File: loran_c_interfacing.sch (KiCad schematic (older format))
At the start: 17 parts, among them P401 SPI Bus A, P402 SPI Bus B, U103 74AC14, U401 74AC14, U402 74AC14

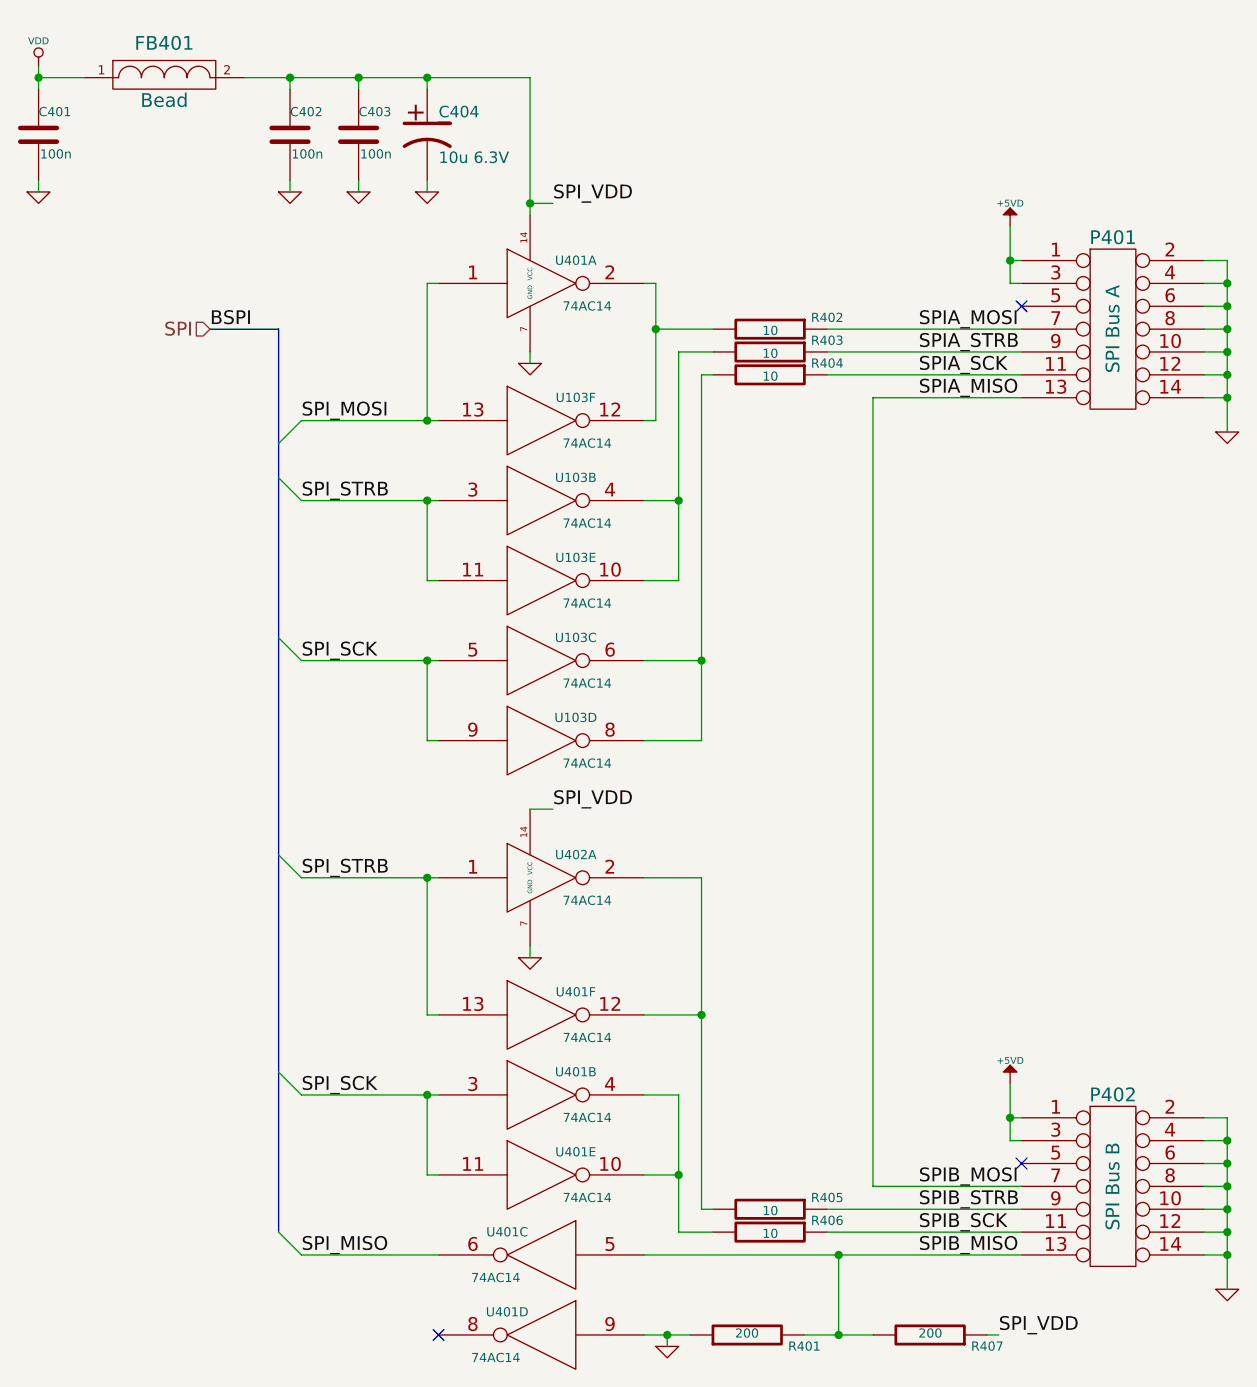
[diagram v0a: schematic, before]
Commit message: FIXED: no more buses on hierarchical sheet ports
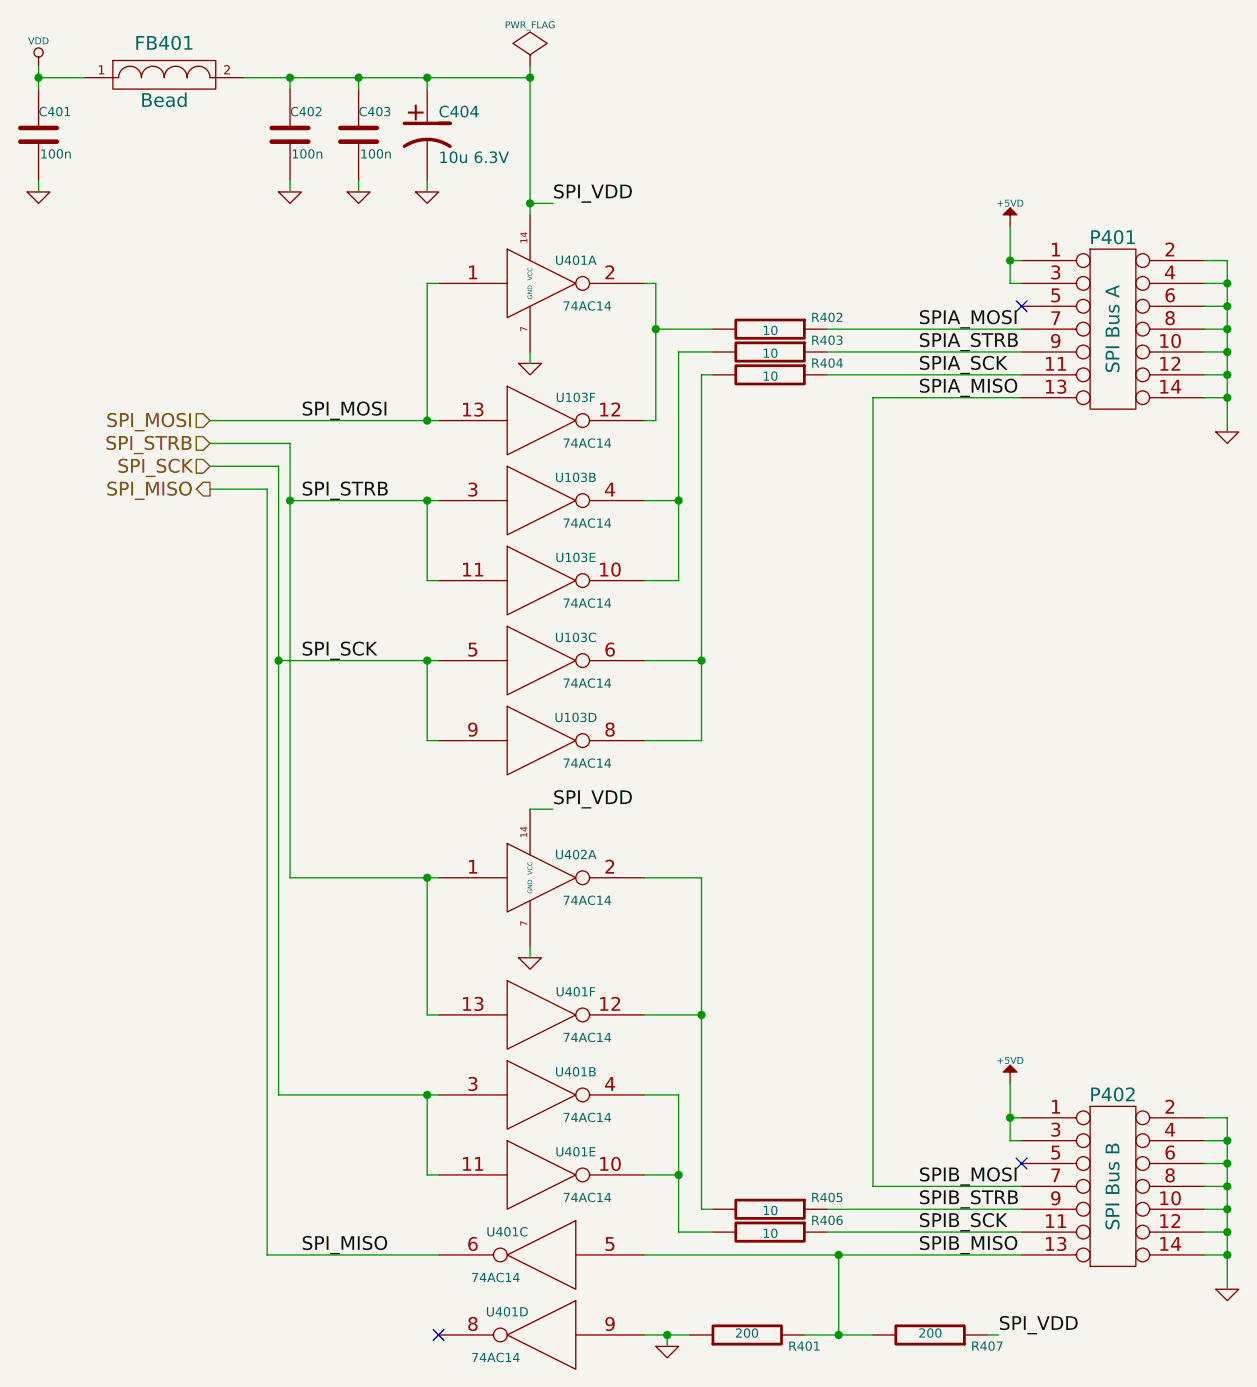
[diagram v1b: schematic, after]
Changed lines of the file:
@@
 $Descr A4 11693 8268
 encoding utf-8
-Sheet 4 7
+Sheet 3 7
 Title ""
 Date ""
@@
 $EndComp
 $Comp
-L GND #PWR066
+L GND #PWR058
 U 1 1 52DAD917
 P 8600 2350
-F 0 "#PWR066" H 8600 2350 30  0001 C CNN
+F 0 "#PWR058" H 8600 2350 30  0001 C CNN
 F 1 "GND" H 8600 2280 30  0001 C CNN
 F 2 "" H 8600 2350 60  0000 C CNN
@@
 $EndComp
 $Comp
-L +5VD #PWR067
+L +5VD #PWR059
 U 1 1 52DAE845
 P 7650 1450
-F 0 "#PWR067" H 7650 1400 20  0001 C CNN
+F 0 "#PWR059" H 7650 1400 20  0001 C CNN
 F 1 "+5VD" H 7650 1550 30  0000 C CNN
 F 2 "" H 7650 1450 60  0000 C CNN
@@
 $EndComp
 $Comp
-L GND #PWR068
+L GND #PWR060
 U 1 1 52DAF90C
 P 8600 6100
-F 0 "#PWR068" H 8600 6100 30  0001 C CNN
+F 0 "#PWR060" H 8600 6100 30  0001 C CNN
 F 1 "GND" H 8600 6030 30  0001 C CNN
 F 2 "" H 8600 6100 60  0000 C CNN
@@
 $EndComp
 $Comp
-L +5VD #PWR069
+L +5VD #PWR061
 U 1 1 52DAF91B
 P 7650 5200
-F 0 "#PWR069" H 7650 5150 20  0001 C CNN
+F 0 "#PWR061" H 7650 5150 20  0001 C CNN
 F 1 "+5VD" H 7650 5300 30  0000 C CNN
 F 2 "" H 7650 5200 60  0000 C CNN
@@
 $EndComp
 $Comp
-L GND #PWR070
+L GND #PWR062
 U 1 1 52DD7CC9
 P 5550 2050
-F 0 "#PWR070" H 5550 2050 30  0001 C CNN
+F 0 "#PWR062" H 5550 2050 30  0001 C CNN
 F 1 "GND" H 5550 1980 30  0001 C CNN
 F 2 "" H 5550 2050 60  0000 C CNN
@@
 $EndComp
 $Comp
-L GND #PWR071
+L GND #PWR063
 U 1 1 52DD892D
 P 5550 4650
-F 0 "#PWR071" H 5550 4650 30  0001 C CNN
+F 0 "#PWR063" H 5550 4650 30  0001 C CNN
 F 1 "GND" H 5550 4580 30  0001 C CNN
 F 2 "" H 5550 4650 60  0000 C CNN
@@
 $EndComp
 $Comp
-L GND #PWR072
+L GND #PWR064
 U 1 1 52DD8B76
 P 6150 6350
-F 0 "#PWR072" H 6150 6350 30  0001 C CNN
+F 0 "#PWR064" H 6150 6350 30  0001 C CNN
 F 1 "GND" H 6150 6280 30  0001 C CNN
 F 2 "" H 6150 6350 60  0000 C CNN
@@
 $EndComp
 $Comp
-L VDD #PWR073
+L VDD #PWR065
 U 1 1 52DDD53B
 P 3400 750
-F 0 "#PWR073" H 3400 850 30  0001 C CNN
+F 0 "#PWR065" H 3400 850 30  0001 C CNN
 F 1 "VDD" H 3400 860 30  0000 C CNN
 F 2 "" H 3400 750 60  0000 C CNN
@@
 $EndComp
 $Comp
-L GND #PWR074
+L GND #PWR066
 U 1 1 52DDD665
 P 3400 1300
-F 0 "#PWR074" H 3400 1300 30  0001 C CNN
+F 0 "#PWR066" H 3400 1300 30  0001 C CNN
 F 1 "GND" H 3400 1230 30  0001 C CNN
 F 2 "" H 3400 1300 60  0000 C CNN
@@
 $EndComp
 $Comp
-L GND #PWR075
+L GND #PWR067
 U 1 1 52DDDBEB
 P 4500 1300
-F 0 "#PWR075" H 4500 1300 30  0001 C CNN
+F 0 "#PWR067" H 4500 1300 30  0001 C CNN
 F 1 "GND" H 4500 1230 30  0001 C CNN
 F 2 "" H 4500 1300 60  0000 C CNN
@@
 $EndComp
 $Comp
-L GND #PWR076
+L GND #PWR068
 U 1 1 52DDDCDD
 P 5100 1300
-F 0 "#PWR076" H 5100 1300 30  0001 C CNN
+F 0 "#PWR068" H 5100 1300 30  0001 C CNN
 F 1 "GND" H 5100 1230 30  0001 C CNN
 F 2 "" H 5100 1300 60  0000 C CNN
@@
 $EndComp
 $Comp
-L GND #PWR077
+L GND #PWR069
 U 1 1 52DDE27D
 P 4800 1300
-F 0 "#PWR077" H 4800 1300 30  0001 C CNN
+F 0 "#PWR069" H 4800 1300 30  0001 C CNN
 F 1 "GND" H 4800 1230 30  0001 C CNN
 F 2 "" H 4800 1300 60  0000 C CNN
@@
 	1    0    0    -1
 $EndComp
-Text Label 4150 1900 0    60   ~ 0
-BSPI
-Text HLabel 4150 1900 0    60   Input ~ 0
-SPI
-Entry Wire Line
-	4450 5850 4550 5950
-Entry Wire Line
-	4450 5150 4550 5250
-Entry Wire Line
-	4450 4200 4550 4300
-Entry Wire Line
-	4450 2550 4550 2650
-Entry Wire Line
-	4450 3250 4550 3350
-Entry Wire Line
-	4450 2400 4550 2300
+Text HLabel 4150 2300 0    60   Input ~ 0
+SPI_MOSI
 Text Label 4550 2300 0    60   ~ 0
 SPI_MOSI
@@
 Text Label 4550 3350 0    60   ~ 0
 SPI_SCK
-Text Label 4550 4300 0    60   ~ 0
-SPI_STRB
-Text Label 4550 5250 0    60   ~ 0
-SPI_SCK
 Text Label 4550 5950 0    60   ~ 0
 SPI_MISO
@@
 	5550 2000 5550 2050
 Wire Wire Line
-	5550 800  5550 1400
+	5550 750  5550 1400
 Wire Wire Line
 	5550 1350 5650 1350
@@
 	6200 5250 6200 5850
 Wire Wire Line
-	4550 4300 5150 4300
+	4500 4300 5150 4300
 Wire Wire Line
 	5100 4300 5100 4900
@@
 	5100 4900 5150 4900
 Wire Wire Line
-	4550 5250 5150 5250
+	4450 5250 5150 5250
 Wire Wire Line
 	5100 5250 5100 5600
@@
 	5100 1700 5100 2300
 Wire Wire Line
-	4550 2300 5150 2300
+	4150 2300 5150 2300
 Wire Wire Line
 	6050 2650 6200 2650
@@
 	6300 3700 6050 3700
 Wire Wire Line
-	4550 2650 5150 2650
+	4500 2650 5150 2650
 Wire Wire Line
 	5100 2650 5100 3000
@@
 	5100 3000 5150 3000
 Wire Wire Line
-	4550 3350 5150 3350
+	4450 3350 5150 3350
 Wire Wire Line
 	5100 3350 5100 3700
@@
 Connection ~ 6900 5950
 Wire Wire Line
-	4550 5950 5150 5950
+	4400 5950 5150 5950
 Wire Wire Line
 	3400 750  3400 850
@@
 	4800 800  4800 850
 Connection ~ 4800 800
-Wire Bus Line
-	4450 1900 4450 5850
-Wire Bus Line
-	4450 1900 4150 1900
 Connection ~ 5100 2300
 Connection ~ 5100 2650
@@
 Connection ~ 5100 4300
 Connection ~ 5100 5250
+Text HLabel 4150 2400 0    60   Input ~ 0
+SPI_STRB
+Text HLabel 4150 2500 0    60   Input ~ 0
+SPI_SCK
+Text HLabel 4150 2600 0    60   Output ~ 0
+SPI_MISO
+Wire Wire Line
+	4150 2400 4500 2400
+Wire Wire Line
+	4500 2400 4500 4300
+Wire Wire Line
+	4150 2500 4450 2500
+Wire Wire Line
+	4450 2500 4450 5250
+Wire Wire Line
+	4150 2600 4400 2600
+Wire Wire Line
+	4400 2600 4400 5950
+Connection ~ 4500 2650
+Connection ~ 4450 3350
+$Comp
+L PWR_FLAG #FLG070
+U 1 1 52E83610
+P 5550 750
+F 0 "#FLG070" H 5550 845 30  0001 C CNN
+F 1 "PWR_FLAG" H 5550 930 30  0000 C CNN
+F 2 "" H 5550 750 60  0000 C CNN
+F 3 "" H 5550 750 60  0000 C CNN
+	1    5550 750
+	1    0    0    -1
+$EndComp
+Connection ~ 5550 800
 $EndSCHEMATC

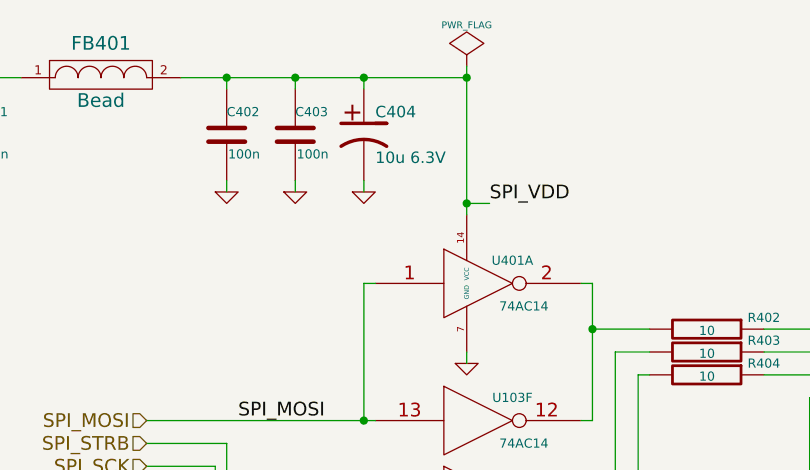
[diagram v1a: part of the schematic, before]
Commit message: Update: fix, assign modules to components -Fix P302 incorrect connection -Assign footprints to components (not all yet) -Back-import footprints into schematic fields
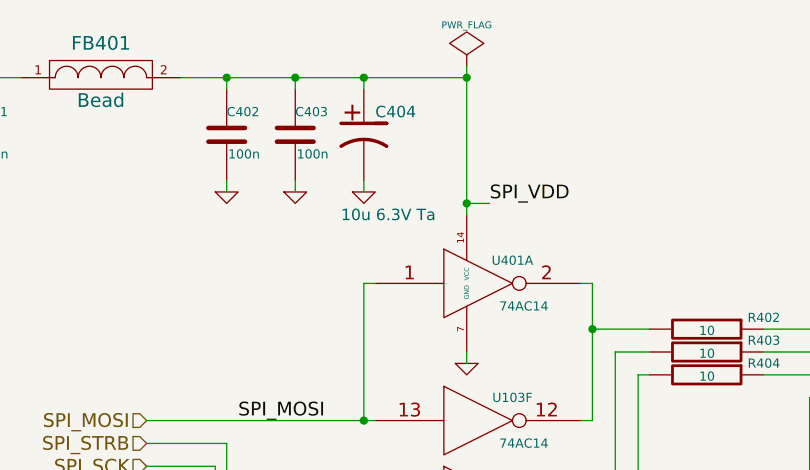
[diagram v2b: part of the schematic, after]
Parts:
- C401, C402, C403: footprint (none) -> w_smd_capacitors:c_1206
- C404: value 10u 6.3V -> 10u 6.3V Ta; footprint (none) -> w_smd_capacitors:c_tant_B
- FB401: footprint (none) -> w_pth_resistors:RC07
- P401, P402: footprint (none) -> w_conn_strip:vasch_strip_7x2
- R401, R402, R403, R404, R405, R406, R407: footprint (none) -> w_smd_resistors:r_1206
- U103, U401, U402: footprint (none) -> w_smd_dil:so-16
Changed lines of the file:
@@
 encoding utf-8
 Sheet 3 7
-Title ""
+Title "SPI interface"
 Date ""
 Rev ""
-Comp "Roman Dobrodiy"
+Comp "Roman Dobrodiy (aka RomaVis)"
 Comment1 ""
 Comment2 ""
@@
 F 0 "P401" H 8100 2300 60  0000 C CNN
 F 1 "SPI Bus A" V 8100 1900 60  0000 C CNN
-F 2 "" H 8100 1900 60  0000 C CNN
+F 2 "w_conn_strip:vasch_strip_7x2" H 8100 1900 60  0001 C CNN
 F 3 "" H 8100 1900 60  0000 C CNN
 	1    8100 1900
@@
 F 0 "P402" H 8100 6050 60  0000 C CNN
 F 1 "SPI Bus B" V 8100 5650 60  0000 C CNN
-F 2 "" H 8100 5650 60  0000 C CNN
+F 2 "w_conn_strip:vasch_strip_7x2" H 8100 5650 60  0001 C CNN
 F 3 "" H 8100 5650 60  0000 C CNN
 	1    8100 5650
@@
 F 0 "U401" H 5750 1800 40  0000 C CNN
 F 1 "74AC14" H 5800 1600 40  0000 C CNN
-F 2 "" H 5600 1700 60  0000 C CNN
+F 2 "w_smd_dil:so-16" H 5600 1700 60  0001 C CNN
 F 3 "" H 5600 1700 60  0000 C CNN
 	1    5600 1700
@@
 F 0 "U103" H 5750 2400 40  0000 C CNN
 F 1 "74AC14" H 5800 2200 40  0000 C CNN
-F 2 "" H 5600 2300 60  0000 C CNN
+F 2 "w_smd_dil:so-16" H 5600 2300 60  0001 C CNN
 F 3 "" H 5600 2300 60  0000 C CNN
 	6    5600 2300
@@
 F 0 "U103" H 5750 2750 40  0000 C CNN
 F 1 "74AC14" H 5800 2550 40  0000 C CNN
-F 2 "" H 5600 2650 60  0000 C CNN
+F 2 "w_smd_dil:so-16" H 5600 2650 60  0001 C CNN
 F 3 "" H 5600 2650 60  0000 C CNN
 	2    5600 2650
@@
 F 0 "U103" H 5750 3100 40  0000 C CNN
 F 1 "74AC14" H 5800 2900 40  0000 C CNN
-F 2 "" H 5600 3000 60  0000 C CNN
+F 2 "w_smd_dil:so-16" H 5600 3000 60  0001 C CNN
 F 3 "" H 5600 3000 60  0000 C CNN
 	5    5600 3000
@@
 F 0 "U103" H 5750 3450 40  0000 C CNN
 F 1 "74AC14" H 5800 3250 40  0000 C CNN
-F 2 "" H 5600 3350 60  0000 C CNN
+F 2 "w_smd_dil:so-16" H 5600 3350 60  0001 C CNN
 F 3 "" H 5600 3350 60  0000 C CNN
 	3    5600 3350
@@
 F 0 "U103" H 5750 3800 40  0000 C CNN
 F 1 "74AC14" H 5800 3600 40  0000 C CNN
-F 2 "" H 5600 3700 60  0000 C CNN
+F 2 "w_smd_dil:so-16" H 5600 3700 60  0001 C CNN
 F 3 "" H 5600 3700 60  0000 C CNN
 	4    5600 3700
@@
 F 0 "U402" H 5750 4400 40  0000 C CNN
 F 1 "74AC14" H 5800 4200 40  0000 C CNN
-F 2 "" H 5600 4300 60  0000 C CNN
+F 2 "w_smd_dil:so-16" H 5600 4300 60  0001 C CNN
 F 3 "" H 5600 4300 60  0000 C CNN
 	1    5600 4300
@@
 F 0 "U401" H 5750 5000 40  0000 C CNN
 F 1 "74AC14" H 5800 4800 40  0000 C CNN
-F 2 "" H 5600 4900 60  0000 C CNN
+F 2 "w_smd_dil:so-16" H 5600 4900 60  0001 C CNN
 F 3 "" H 5600 4900 60  0000 C CNN
 	6    5600 4900
@@
 F 0 "U401" H 5750 5350 40  0000 C CNN
 F 1 "74AC14" H 5800 5150 40  0000 C CNN
-F 2 "" H 5600 5250 60  0000 C CNN
+F 2 "w_smd_dil:so-16" H 5600 5250 60  0001 C CNN
 F 3 "" H 5600 5250 60  0000 C CNN
 	2    5600 5250
@@
 F 0 "U401" H 5750 5700 40  0000 C CNN
 F 1 "74AC14" H 5800 5500 40  0000 C CNN
-F 2 "" H 5600 5600 60  0000 C CNN
+F 2 "w_smd_dil:so-16" H 5600 5600 60  0001 C CNN
 F 3 "" H 5600 5600 60  0000 C CNN
 	5    5600 5600
@@
 F 0 "U401" H 5750 6050 40  0000 C CNN
 F 1 "74AC14" H 5800 5850 40  0000 C CNN
-F 2 "" H 5600 5950 60  0000 C CNN
+F 2 "w_smd_dil:so-16" H 5600 5950 60  0001 C CNN
 F 3 "" H 5600 5950 60  0000 C CNN
 	3    5600 5950
@@
 F 0 "U401" H 5750 6400 40  0000 C CNN
 F 1 "74AC14" H 5800 6200 40  0000 C CNN
-F 2 "" H 5600 6300 60  0000 C CNN
+F 2 "w_smd_dil:so-16" H 5600 6300 60  0001 C CNN
 F 3 "" H 5600 6300 60  0000 C CNN
 	4    5600 6300
@@
 F 0 "R405" V 6550 6000 40  0000 C CNN
 F 1 "10" V 6607 5751 40  0000 C CNN
-F 2 "" V 6530 5750 30  0000 C CNN
+F 2 "w_smd_resistors:r_1206" V 6530 5750 30  0001 C CNN
 F 3 "" H 6600 5750 30  0000 C CNN
 	1    6600 5750
@@
 F 0 "R406" V 6550 6100 40  0000 C CNN
 F 1 "10" V 6607 5851 40  0000 C CNN
-F 2 "" V 6530 5850 30  0000 C CNN
+F 2 "w_smd_resistors:r_1206" V 6530 5850 30  0001 C CNN
 F 3 "" H 6600 5850 30  0000 C CNN
 	1    6600 5850
@@
 F 0 "R407" V 7250 6550 40  0000 C CNN
 F 1 "200" V 7307 6301 40  0000 C CNN
-F 2 "" V 7230 6300 30  0000 C CNN
+F 2 "w_smd_resistors:r_1206" V 7230 6300 30  0001 C CNN
 F 3 "" H 7300 6300 30  0000 C CNN
 	1    7300 6300
@@
 F 0 "R401" V 6450 6050 40  0000 C CNN
 F 1 "200" V 6507 6301 40  0000 C CNN
-F 2 "" V 6430 6300 30  0000 C CNN
+F 2 "w_smd_resistors:r_1206" V 6430 6300 30  0001 C CNN
 F 3 "" H 6500 6300 30  0000 C CNN
 	1    6500 6300
@@
 F 0 "R404" V 6550 2350 40  0000 C CNN
 F 1 "10" V 6607 2101 40  0000 C CNN
-F 2 "" V 6530 2100 30  0000 C CNN
+F 2 "w_smd_resistors:r_1206" V 6530 2100 30  0001 C CNN
 F 3 "" H 6600 2100 30  0000 C CNN
 	1    6600 2100
@@
 F 0 "R403" V 6550 2250 40  0000 C CNN
 F 1 "10" V 6607 2001 40  0000 C CNN
-F 2 "" V 6530 2000 30  0000 C CNN
+F 2 "w_smd_resistors:r_1206" V 6530 2000 30  0001 C CNN
 F 3 "" H 6600 2000 30  0000 C CNN
 	1    6600 2000
@@
 F 0 "R402" V 6550 2150 40  0000 C CNN
 F 1 "10" V 6607 1901 40  0000 C CNN
-F 2 "" V 6530 1900 30  0000 C CNN
+F 2 "w_smd_resistors:r_1206" V 6530 1900 30  0001 C CNN
 F 3 "" H 6600 1900 30  0000 C CNN
 	1    6600 1900
@@
 F 0 "C401" H 3400 1150 40  0000 L CNN
 F 1 "100n" H 3406 965 40  0000 L CNN
-F 2 "" H 3438 900 30  0000 C CNN
+F 2 "w_smd_capacitors:c_1206" H 3438 900 30  0001 C CNN
 F 3 "" H 3400 1050 60  0000 C CNN
 	1    3400 1050
@@
 F 0 "FB401" H 3950 950 60  0000 C CNN
 F 1 "Bead" H 3950 700 60  0000 C CNN
-F 2 "" H 3950 800 60  0000 C CNN
+F 2 "w_pth_resistors:RC07" H 3950 800 60  0001 C CNN
 F 3 "" H 3950 800 60  0000 C CNN
 	1    3950 800
@@
 F 0 "C402" H 4500 1150 40  0000 L CNN
 F 1 "100n" H 4506 965 40  0000 L CNN
-F 2 "" H 4538 900 30  0000 C CNN
+F 2 "w_smd_capacitors:c_1206" H 4538 900 30  0001 C CNN
 F 3 "" H 4500 1050 60  0000 C CNN
 	1    4500 1050
@@
 P 5100 1050
 F 0 "C404" H 5150 1150 50  0000 L CNN
-F 1 "10u 6.3V" H 5150 950 50  0000 L CNN
-F 2 "" H 5100 1050 60  0000 C CNN
+F 1 "10u 6.3V Ta" H 5000 700 50  0000 L CNN
+F 2 "w_smd_capacitors:c_tant_B" H 5100 1050 60  0001 C CNN
 F 3 "" H 5100 1050 60  0000 C CNN
 	1    5100 1050
@@
 F 0 "C403" H 4800 1150 40  0000 L CNN
 F 1 "100n" H 4806 965 40  0000 L CNN
-F 2 "" H 4838 900 30  0000 C CNN
+F 2 "w_smd_capacitors:c_1206" H 4838 900 30  0001 C CNN
 F 3 "" H 4800 1050 60  0000 C CNN
 	1    4800 1050
